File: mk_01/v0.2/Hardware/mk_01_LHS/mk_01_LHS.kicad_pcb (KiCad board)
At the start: 2 copper layers, 79 parts, among them SW1 SW_Push_Dual, U1 nice_nano

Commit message: LED removal and progress
The LEDs have been removed from the schematic and the board design, edge cuts and routing for the key matrix have been added, as has the capacitor|resistor layout for the rotary encoder (which I may replace with an ec11 for push button functionality). The other components have also been arranged into their correct positions.
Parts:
- C7, C8: footprint Capacitor_SMD:C_0402_1005Metric_Pad0.74x0.62mm_HandSolder -> Capacitor_SMD:C_0805_2012Metric_Pad1.18x1.45mm_HandSolder; moved to B.Cu
- MX1, MX10, MX11, MX12, MX13, MX14, MX15, MX16, MX17, MX18, MX19, MX2, MX20, MX21, MX22, MX23, MX24, MX25, MX26, MX27, MX28, MX29, MX3, MX30, MX31, MX32, MX33, MX34, MX4, MX5, MX6, MX7, MX8, MX9: value MX-LED -> MX-NoLED; footprint MX_Only:MXOnly-1U-Hotswap -> MX_Only:MXOnly-1U-Hotswap-NoLED
- R1, R2, R3, R4: footprint Resistor_SMD:R_0201_0603Metric_Pad0.64x0.40mm_HandSolder -> Resistor_SMD:R_0805_2012Metric_Pad1.20x1.40mm_HandSolder; moved to B.Cu
- moved OLED1 151.2 mm to (178.4, 74.3)
- moved D_6 138.4 mm to (162.6, 48.3), turned to 90 degrees
- moved BATT1 131.4 mm to (178.4, 93.0), turned to -90 degrees
- moved D_5 122.2 mm to (143.5, 48.3), turned to 90 degrees
- moved D_13 117.9 mm to (162.6, 67.3), turned to 90 degrees
- moved D_3 114.6 mm to (105.4, 48.3), turned to 90 degrees
- moved D_20 114.5 mm to (162.6, 86.4), turned to 90 degrees
- moved D_4 109.2 mm to (124.5, 48.3), turned to 90 degrees
- moved D_12 108.0 mm to (143.5, 67.3), turned to 90 degrees
- moved D_11 91.7 mm to (124.5, 67.3), turned to 90 degrees
- moved D_27 89.3 mm to (162.6, 105.4), turned to 90 degrees
- moved D_7 88.6 mm to (48.3, 67.3), turned to 90 degrees
- moved D_10 88.0 mm to (105.4, 67.3), turned to 90 degrees
- moved D_34 87.0 mm to (162.6, 124.5), turned to 90 degrees
- moved D_8 84.9 mm to (67.3, 67.3), turned to 90 degrees
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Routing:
- net row4: track 0.00 -> 114.3 mm
- net row3: track 0.00 -> 114.3 mm
- net row2: track 0.00 -> 114.3 mm
- net row1: track 0.00 -> 114.3 mm
- net row0: track 19.0 -> 95.2 mm
- net col6: track 0.00 -> 76.2 mm, vias 0 -> 5
- net col5: track 0.00 -> 76.2 mm, vias 0 -> 5
- net col4: track 0.00 -> 76.2 mm, vias 0 -> 5
- net col3: track 0.00 -> 76.2 mm, vias 0 -> 5
- net col2: track 0.00 -> 76.2 mm, vias 0 -> 5
- net col0: track 0.00 -> 57.2 mm
- net VCC: track 0.00 -> 34.9 mm
- net Net-(OLED1-Pad4): track 0.00 -> 15.0 mm
- net Net-(OLED1-Pad3): track 0.00 -> 13.9 mm
- net Net-(R1-Pad2): track 0.00 -> 11.1 mm
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- added copper zone on B.Cu, net GND
- added copper zone on F.Cu, net GND
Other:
- board outline added: 165.1 x 102.9 mm

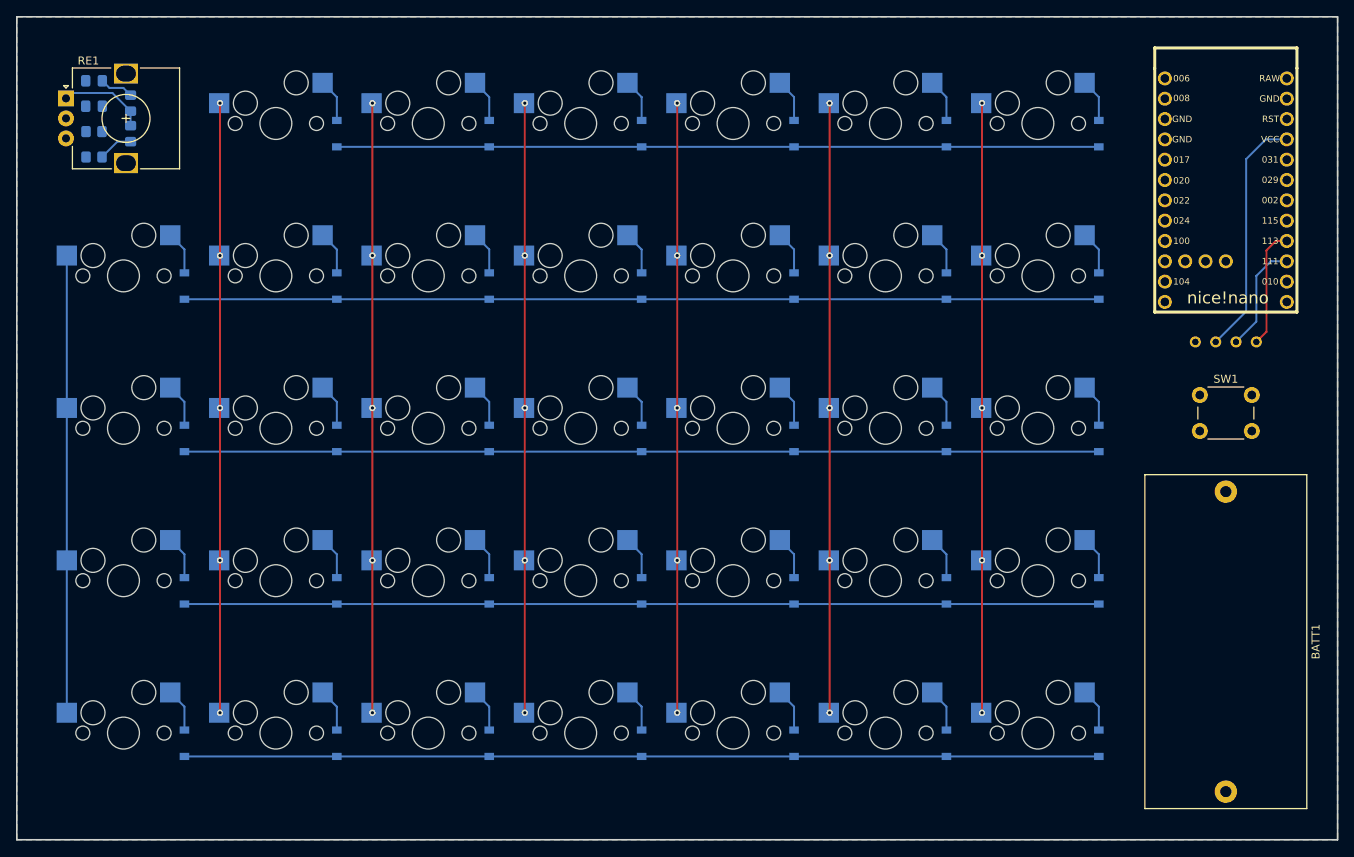
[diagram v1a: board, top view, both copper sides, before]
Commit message: Updated PCB design
The PCB design has been updated and is now relatively complete. The hardware is fully MIT compliant, as all libraries used are under MIT license, and the design is entirely my own. Now it's time to round the tracks. The schematic has been lightly updated too based on the PCB design (changing a few connections to make routing the board simpler).
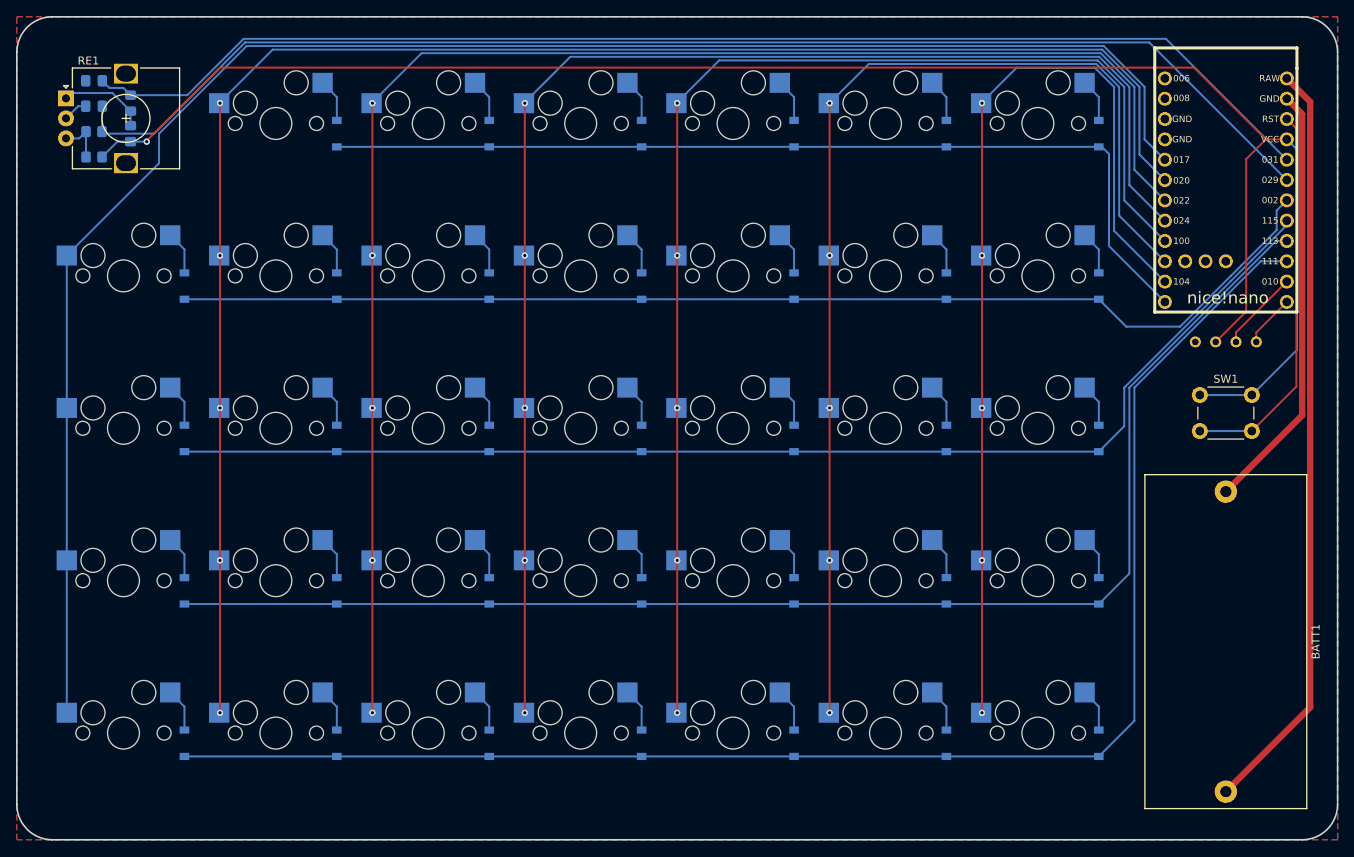
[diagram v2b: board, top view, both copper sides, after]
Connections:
- BATT1 pad 1: Net-(BATT1-Pad1) -> Net-(U1-Pad23)
- BATT1 pad 2: Net-(BATT1-Pad2) -> Net-(U1-Pad24)
- C7 pad 1: GND -> Earth
- C8 pad 2: GND -> Earth
- OLED1 pad 1: GND -> Earth
- RE1 pad C: GND -> Earth
- SW1 pad 1: GND -> VCC
- U1 pad 10: unconnected-(U1-Pad10) -> col5
- U1 pad 11: unconnected-(U1-Pad11) -> col6
- U1 pad 12: unconnected-(U1-Pad12) -> row0
- U1 pad 13: unconnected-(U1-Pad13) -> Net-(OLED1-Pad4)
- U1 pad 14: unconnected-(U1-Pad14) -> Net-(OLED1-Pad3)
- U1 pad 15: Net-(OLED1-Pad3) -> row4
- U1 pad 16: Net-(OLED1-Pad4) -> row3
- U1 pad 17: unconnected-(U1-Pad17) -> row2
- U1 pad 18: unconnected-(U1-Pad18) -> row1
- U1 pad 23: Net-(BATT1-Pad2) -> Net-(U1-Pad23)
- U1 pad 24: Net-(BATT1-Pad1) -> Net-(U1-Pad24)
- U1 pad 5: unconnected-(U1-Pad5) -> col0
- U1 pad 6: unconnected-(U1-Pad6) -> col1
- U1 pad 7: unconnected-(U1-Pad7) -> col2
- U1 pad 8: unconnected-(U1-Pad8) -> col3
- U1 pad 9: unconnected-(U1-Pad9) -> col4
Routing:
- net VCC: track 34.9 -> 225.7 mm, vias 0 -> 1
- net Net-(C8-Pad1): track 0.05 -> 163.2 mm
- net col0: track 57.2 -> 217.2 mm
- net Net-(C7-Pad2): track 4.46 -> 158.2 mm
- net col1: track 76.2 -> 208.9 mm
- net col2: track 76.2 -> 191.6 mm
- net col3: track 76.2 -> 174.4 mm
- net Net-(U1-Pad24): track 0.00 -> 94.7 mm
- net col4: track 76.2 -> 157.1 mm
- net row4: track 114.3 -> 187.8 mm
- net col5: track 76.2 -> 140.9 mm
- net row3: track 114.3 -> 170.2 mm
- net Net-(U1-Pad23): track 0.00 -> 53.9 mm
- net Net-(SW1-Pad2): track 0.00 -> 48.3 mm
- net col6: track 76.2 -> 122.6 mm
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- added copper zone on B.Cu, net Earth
- added copper zone on F.Cu, net Earth
- removed copper zone on B.Cu, net GND
- removed copper zone on F.Cu, net GND
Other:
- outline, holes or cut-outs redrawn
